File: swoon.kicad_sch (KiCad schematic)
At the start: 93 parts, among them J1 3305-0-15-80-47-27-10-0, J10 3305-0-15-80-47-27-10-0, J11 3305-0-15-80-47-27-10-0, J12 3305-0-15-80-47-27-10-0, J13 3305-0-15-80-47-27-10-0, J14 3305-0-15-80-47-27-10-0, J15 3305-0-15-80-47-27-10-0, J16 3305-0-15-80-47-27-10-0, J17 3305-0-15-80-47-27-10-0, J18 3305-0-15-80-47-27-10-0, J19 3305-0-15-80-47-27-10-0, J2 3305-0-15-80-47-27-10-0, J20 3305-0-15-80-47-27-10-0, J21 3305-0-15-80-47-27-10-0, J22 3305-0-15-80-47-27-10-0, J23 3305-0-15-80-47-27-10-0, J24 3305-0-15-80-47-27-10-0, J25 3305-0-15-80-47-27-10-0, J26 3305-0-15-80-47-27-10-0, J27 3305-0-15-80-47-27-10-0, J28 3305-0-15-80-47-27-10-0, J29 3305-0-15-80-47-27-10-0, J3 3305-0-15-80-47-27-10-0, J30 3305-0-15-80-47-27-10-0, J31 3305-0-15-80-47-27-10-0, J32 3305-0-15-80-47-27-10-0, J33 3305-0-15-80-47-27-10-0, J34 3305-0-15-80-47-27-10-0, J35 3305-0-15-80-47-27-10-0, J36 3305-0-15-80-47-27-10-0, J37 3305-0-15-80-47-27-10-0, J38 3305-0-15-80-47-27-10-0, J39 3305-0-15-80-47-27-10-0, J4 3305-0-15-80-47-27-10-0, J40 3305-0-15-80-47-27-10-0, J41 3305-0-15-80-47-27-10-0, J42 3305-0-15-80-47-27-10-0, J43 3305-0-15-80-47-27-10-0, J44 3305-0-15-80-47-27-10-0, J45 3305-0-15-80-47-27-10-0, J46 3305-0-15-80-47-27-10-0, J47 3305-0-15-80-47-27-10-0, J48 3305-0-15-80-47-27-10-0, J49 3305-0-15-80-47-27-10-0, J5 3305-0-15-80-47-27-10-0, J50 3305-0-15-80-47-27-10-0, J51 3305-0-15-80-47-27-10-0, J52 3305-0-15-80-47-27-10-0, J53 3305-0-15-80-47-27-10-0, J54 3305-0-15-80-47-27-10-0, J55 3305-0-15-80-47-27-10-0, J56 3305-0-15-80-47-27-10-0, J57 3305-0-15-80-47-27-10-0, J58 3305-0-15-80-47-27-10-0, J59 3305-0-15-80-47-27-10-0, J6 3305-0-15-80-47-27-10-0, J60 3305-0-15-80-47-27-10-0, J61 3305-0-15-80-47-27-10-0, J62 3305-0-15-80-47-27-10-0, J63 3305-0-15-80-47-27-10-0, J64 3305-0-15-80-47-27-10-0, J65 3305-0-15-80-47-27-10-0, J66 3305-0-15-80-47-27-10-0, J67 3305-0-15-80-47-27-10-0, J68 3305-0-15-80-47-27-10-0, J69 Conn_01x09_Socket, J7 3305-0-15-80-47-27-10-0, J70 Conn_01x09_Socket, J71 Conn_01x02_Socket, J8 3305-0-15-80-47-27-10-0, J9 3305-0-15-80-47-27-10-0, SW1 SW_Push, SW10 SW_Push, SW11 SW_Push, SW12 SW_Push, SW13 SW_Push, SW14 SW_Push, SW15 SW_Push, SW16 SW_Push, SW17 SW_Push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

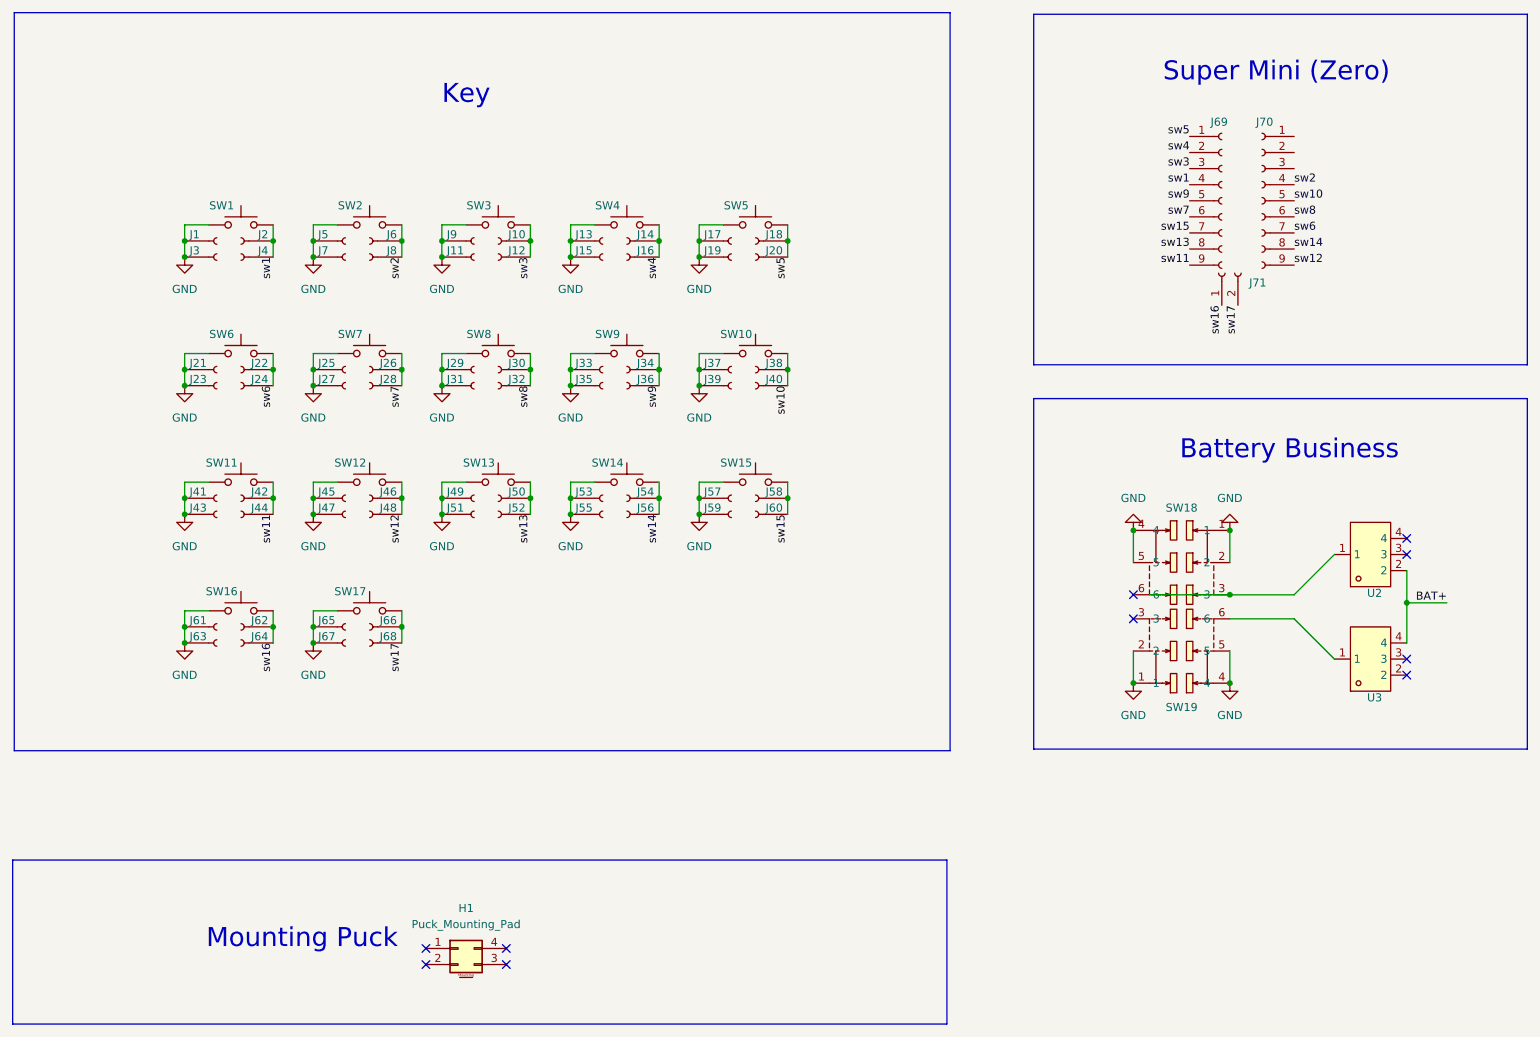
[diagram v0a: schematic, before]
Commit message: Revert "add build123d workflow"
This reverts commit e4690586cedccb0c1d963ceafc7b9e119b231d94.
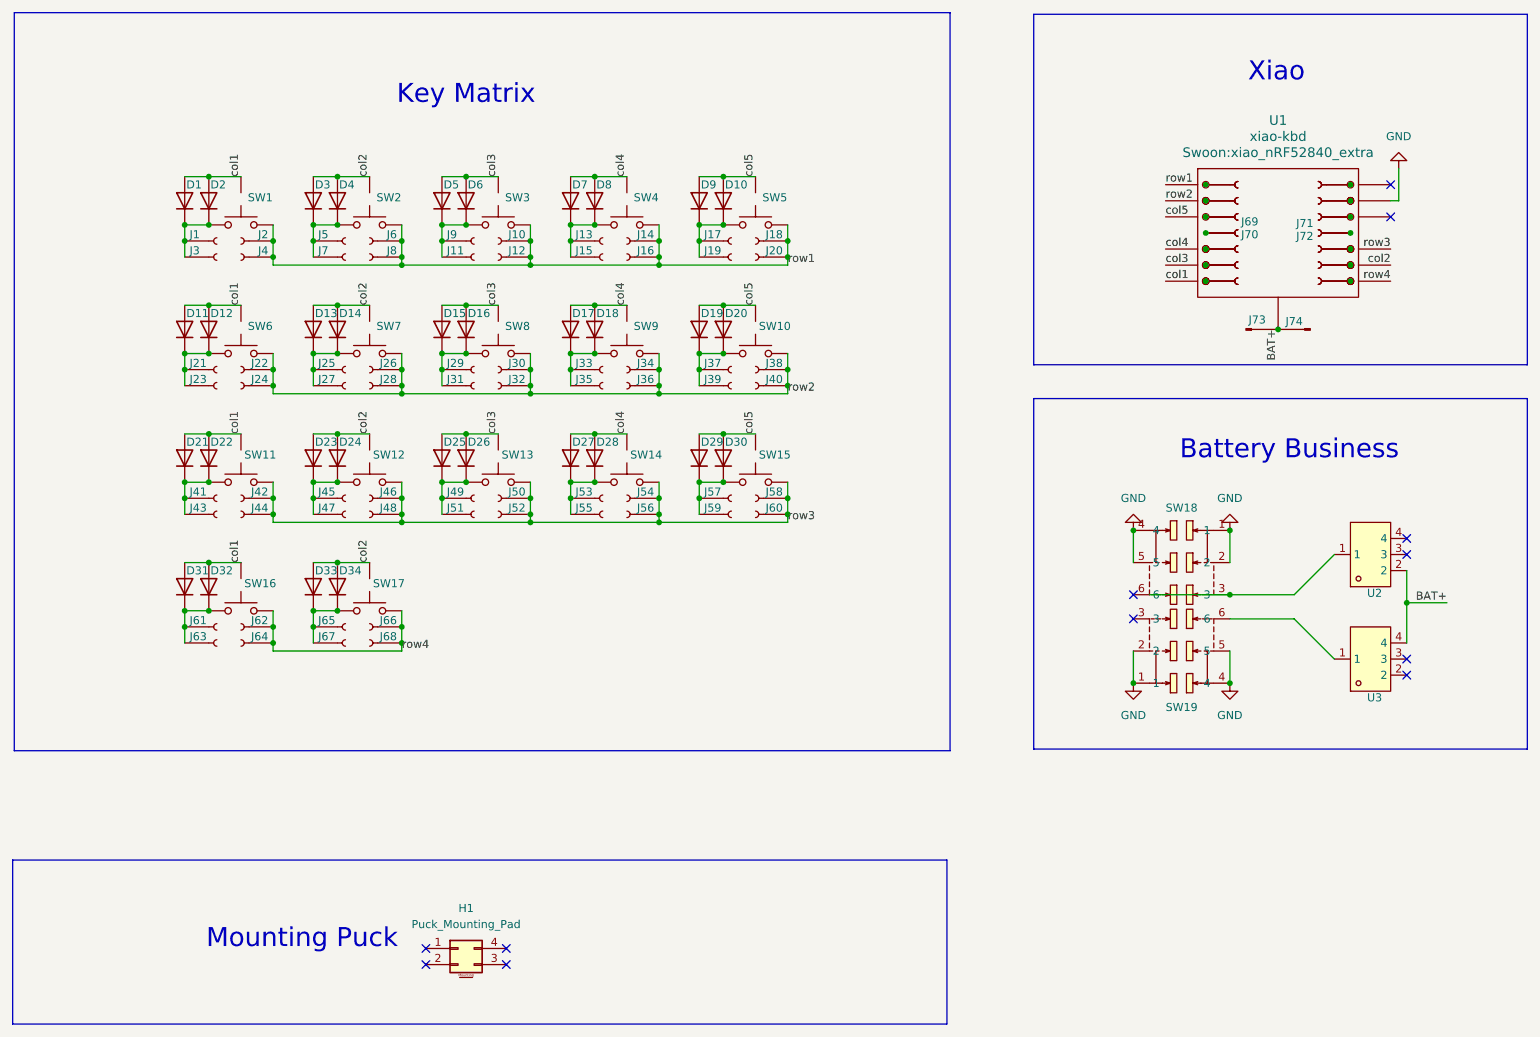
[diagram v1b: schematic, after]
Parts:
- removed J69, J70: Conn_01x09_Socket, Connector_PinHeader_2.54mm:PinHeader_1x09_P2.54mm_Vertical, symbol Connector:Conn_01x09_Socket
- removed J71: Conn_01x02_Socket, Connector_PinHeader_2.54mm:PinHeader_1x02_P2.54mm_Vertical, symbol Connector:Conn_01x02_Socket
- added D1, D10, D11, D12, D13, D14, D15, D16, D17, D18, D19, D2, D20, D21, D22, D23, D24, D25, D26, D27, D28, D29, D3, D30, D31, D32, D33, D34, D4, D5, D6, D7, D8, D9: CD4148WS, Swoon:D_0805_2012Metric, symbol Diode:CD4148W
- added J69, J70, J71, J72: 310-13-107-41-001000, Swoon:MF254V-11-07-0743, symbol Connector:Conn_01x07_Socket
- added J73, J74: Mill Max 0906-2-15-20-75-14-11-0, Swoon:0906-2-15-20-75-14-11-0, symbol Connector:Conn_01x01_Pin
- added TP1, TP10, TP11, TP12, TP13, TP14, TP15, TP16, TP17, TP18, TP19, TP2, TP20, TP3, TP4, TP5, TP6, TP7, TP8, TP9: TestPoint_Small, Swoon:TestPoint_Pad_1.0x1.0mm, symbol Connector:TestPoint_Small
- added U1: xiao-kbd, Swoon:xiao_nRF52840_extra, symbol Swoon:xiao_nRF52840_extra
- SW1, SW10, SW11, SW12, SW13, SW14, SW15, SW16, SW17, SW2, SW3, SW4, SW5, SW6, SW7, SW8, SW9: footprint Swoon:SW_PG1350 -> Swoon:SW_PG1350_vias; symbol Switch:SW_Push -> Swoon:SW_Push; now left out of the parts list
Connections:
- net BAT+: now also J73.1 (Pin_1), J74.1 (Pin_1), U1.15 (BAT+)
- net GND: now also U1.13 (GND); no longer J1.1 (Pin_1), J11.1 (Pin_1), J13.1 (Pin_1), J15.1 (Pin_1), J17.1 (Pin_1), J19.1 (Pin_1), J21.1 (Pin_1), J23.1 (Pin_1), J25.1 (Pin_1), J27.1 (Pin_1), J29.1 (Pin_1), J3.1 (Pin_1), J31.1 (Pin_1), J33.1 (Pin_1), J35.1 (Pin_1), J37.1 (Pin_1), J39.1 (Pin_1), J41.1 (Pin_1), J43.1 (Pin_1), J45.1 (Pin_1), J47.1 (Pin_1), J49.1 (Pin_1), J5.1 (Pin_1), J51.1 (Pin_1), J53.1 (Pin_1), J55.1 (Pin_1), J57.1 (Pin_1), J59.1 (Pin_1), J61.1 (Pin_1), J63.1 (Pin_1), J65.1 (Pin_1), J67.1 (Pin_1), J7.1 (Pin_1), J9.1 (Pin_1), SW1.1, SW10.1, SW11.1, SW12.1, SW13.1, SW14.1, SW15.1, SW16.1, SW17.1, SW2.1, SW3.1, SW4.1, SW5.1, SW6.1, SW7.1, SW8.1, SW9.1
- net sw1 renamed row1
- net row1: now also J10.1 (Pin_1), J12.1 (Pin_1), J14.1 (Pin_1), J16.1 (Pin_1), J18.1 (Pin_1), J20.1 (Pin_1), J6.1 (Pin_1), J8.1 (Pin_1), SW1.1, SW2.1, SW3.1, SW4.1, SW5.1, U1.1 (D0); no longer SW1.2
- net sw10 renamed row2
- net row2: now also J22.1 (Pin_1), J24.1 (Pin_1), J26.1 (Pin_1), J28.1 (Pin_1), J30.1 (Pin_1), J32.1 (Pin_1), J34.1 (Pin_1), J36.1 (Pin_1), SW10.1, SW6.1, SW7.1, SW8.1, SW9.1, U1.2 (D1); no longer SW10.2
- net sw11 renamed row3
- net row3: now also J46.1 (Pin_1), J48.1 (Pin_1), J50.1 (Pin_1), J52.1 (Pin_1), J54.1 (Pin_1), J56.1 (Pin_1), J58.1 (Pin_1), J60.1 (Pin_1), SW11.1, SW12.1, SW13.1, SW14.1, SW15.1, U1.10 (D9); no longer SW11.2
- removed net sw12: J46.1 (Pin_1), J48.1 (Pin_1), SW12.2
- removed net sw13: J50.1 (Pin_1), J52.1 (Pin_1), SW13.2
- removed net sw14: J54.1 (Pin_1), J56.1 (Pin_1), SW14.2
- removed net sw15: J58.1 (Pin_1), J60.1 (Pin_1), SW15.2
- net sw16 renamed row4
- net row4: now also J66.1 (Pin_1), J68.1 (Pin_1), SW16.1, SW17.1, U1.8 (D7); no longer SW16.2
- removed net sw17: J66.1 (Pin_1), J68.1 (Pin_1), SW17.2
- removed net sw2: J6.1 (Pin_1), J8.1 (Pin_1), SW2.2
- removed net sw3: J10.1 (Pin_1), J12.1 (Pin_1), SW3.2
- removed net sw4: J14.1 (Pin_1), J16.1 (Pin_1), SW4.2
- removed net sw5: J18.1 (Pin_1), J20.1 (Pin_1), SW5.2
- removed net sw6: J22.1 (Pin_1), J24.1 (Pin_1), SW6.2
- removed net sw7: J26.1 (Pin_1), J28.1 (Pin_1), SW7.2
- removed net sw8: J30.1 (Pin_1), J32.1 (Pin_1), SW8.2
- removed net sw9: J34.1 (Pin_1), J36.1 (Pin_1), SW9.2
- new net: D31.1 (K), D32.1 (K), J61.1 (Pin_1), J63.1 (Pin_1), SW16.2
- new net: D23.1 (K), D24.1 (K), J45.1 (Pin_1), J47.1 (Pin_1), SW12.2
- new net: J69.1 (Pin_1), J70.1 (Pin_1), TP1.1, U1.16 (hole)
- new net: J69.2 (Pin_2), J70.2 (Pin_2), TP20.1, TP3.1, U1.17 (hole)
- new net: J69.3 (Pin_3), J70.3 (Pin_3), TP5.1, U1.18 (hole)
- new net: J69.4 (Pin_4), J70.4 (Pin_4), U1.19 (hole)
- new net: J69.5 (Pin_5), J70.5 (Pin_5), TP14.1, TP7.1, U1.20 (hole)
- new net: J69.6 (Pin_6), J70.6 (Pin_6), TP16.1, TP9.1, U1.21 (hole)
- new net: J69.7 (Pin_7), J70.7 (Pin_7), TP11.1, TP18.1, U1.22 (hole)
- new net: J71.5 (Pin_5), J72.5 (Pin_5), TP13.1, TP8.1, U1.25 (hole)
- new net: D17.1 (K), D18.1 (K), J33.1 (Pin_1), J35.1 (Pin_1), SW9.2
- new net: D33.1 (K), D34.1 (K), J65.1 (Pin_1), J67.1 (Pin_1), SW17.2
- new net: D19.1 (K), D20.1 (K), J37.1 (Pin_1), J39.1 (Pin_1), SW10.2
- new net: D1.1 (K), D2.1 (K), J1.1 (Pin_1), J3.1 (Pin_1), SW1.2
- new net: D15.1 (K), D16.1 (K), J29.1 (Pin_1), J31.1 (Pin_1), SW8.2
- new net: D29.1 (K), D30.1 (K), J57.1 (Pin_1), J59.1 (Pin_1), SW15.2
- new net: J71.2 (Pin_2), J72.2 (Pin_2), TP19.1, TP4.1, U1.28 (hole)
- new net: D10.1 (K), D9.1 (K), J17.1 (Pin_1), J19.1 (Pin_1), SW5.2
- new net: J71.1 (Pin_1), J72.1 (Pin_1), TP2.1, U1.29 (hole)
- new net: J71.3 (Pin_3), J72.3 (Pin_3), TP6.1, U1.27 (hole)
- new net: J71.4 (Pin_4), J72.4 (Pin_4), U1.26 (hole)
- new net: J71.6 (Pin_6), J72.6 (Pin_6), TP10.1, TP15.1, U1.24 (hole)
- new net: J71.7 (Pin_7), J72.7 (Pin_7), TP12.1, TP17.1, U1.23 (hole)
- new net: D5.1 (K), D6.1 (K), J11.1 (Pin_1), J9.1 (Pin_1), SW3.2
- new net: D27.1 (K), D28.1 (K), J53.1 (Pin_1), J55.1 (Pin_1), SW14.2
- new net: D25.1 (K), D26.1 (K), J49.1 (Pin_1), J51.1 (Pin_1), SW13.2
- new net: D13.1 (K), D14.1 (K), J25.1 (Pin_1), J27.1 (Pin_1), SW7.2
- new net: D3.1 (K), D4.1 (K), J5.1 (Pin_1), J7.1 (Pin_1), SW2.2
- new net: D7.1 (K), D8.1 (K), J13.1 (Pin_1), J15.1 (Pin_1), SW4.2
- new net: D21.1 (K), D22.1 (K), J41.1 (Pin_1), J43.1 (Pin_1), SW11.2
- new net: D11.1 (K), D12.1 (K), J21.1 (Pin_1), J23.1 (Pin_1), SW6.2
- new net col1: D1.2 (A), D11.2 (A), D12.2 (A), D2.2 (A), D21.2 (A), D22.2 (A), D31.2 (A), D32.2 (A), SW1.3, SW11.3, SW16.3, SW6.3, U1.7 (D6)
- new net col2: D13.2 (A), D14.2 (A), D23.2 (A), D24.2 (A), D3.2 (A), D33.2 (A), D34.2 (A), D4.2 (A), SW12.3, SW17.3, SW2.3, SW7.3, U1.9 (D8)
- new net col3: D15.2 (A), D16.2 (A), D25.2 (A), D26.2 (A), D5.2 (A), D6.2 (A), SW13.3, SW3.3, SW8.3, U1.6 (D5)
- new net col4: D17.2 (A), D18.2 (A), D27.2 (A), D28.2 (A), D7.2 (A), D8.2 (A), SW14.3, SW4.3, SW9.3, U1.5 (D4)
- new net col5: D10.2 (A), D19.2 (A), D20.2 (A), D29.2 (A), D30.2 (A), D9.2 (A), SW10.3, SW15.3, SW5.3, U1.3 (D2)
- no-connect marks 10 -> 12
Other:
- note added: "Key Matrix"
- note added: "Xiao"
- note removed: "Key"
- note removed: "Super Mini (Zero)"

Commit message: add build123d workflow
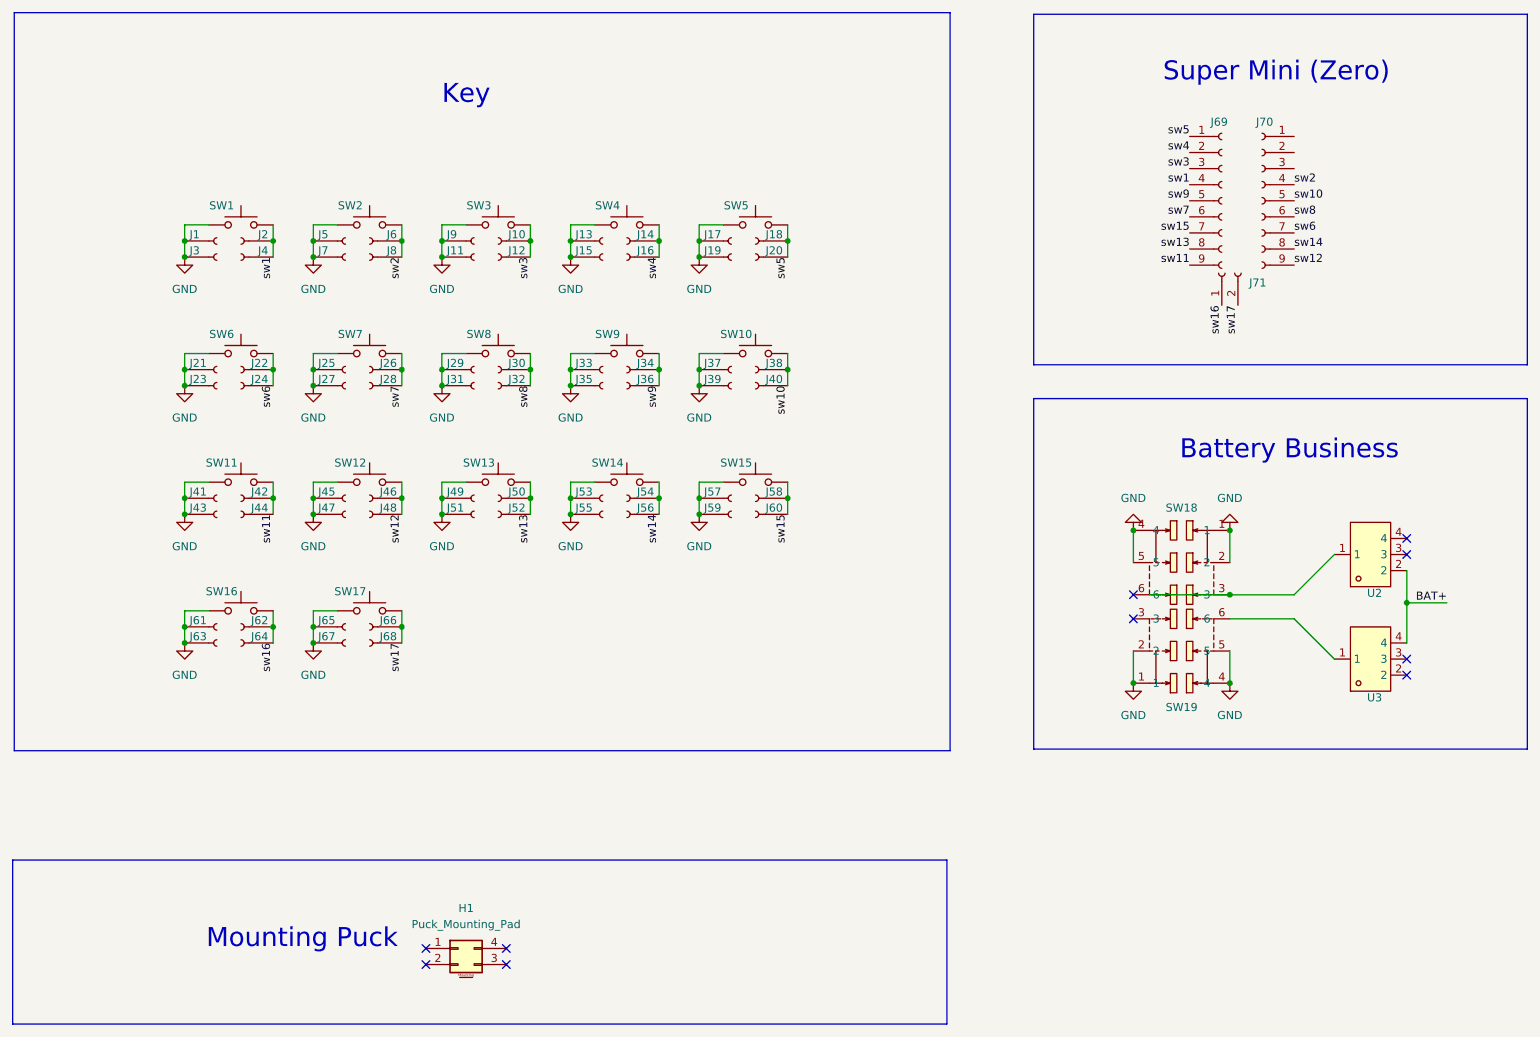
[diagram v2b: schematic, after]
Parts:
- removed D1, D10, D11, D12, D13, D14, D15, D16, D17, D18, D19, D2, D20, D21, D22, D23, D24, D25, D26, D27, D28, D29, D3, D30, D31, D32, D33, D34, D4, D5, D6, D7, D8, D9: CD4148WS, Swoon:D_0805_2012Metric, symbol Diode:CD4148W
- removed J69, J70, J71, J72: 310-13-107-41-001000, Swoon:MF254V-11-07-0743, symbol Connector:Conn_01x07_Socket
- removed J73, J74: Mill Max 0906-2-15-20-75-14-11-0, Swoon:0906-2-15-20-75-14-11-0, symbol Connector:Conn_01x01_Pin
- removed TP1, TP10, TP11, TP12, TP13, TP14, TP15, TP16, TP17, TP18, TP19, TP2, TP20, TP3, TP4, TP5, TP6, TP7, TP8, TP9: TestPoint_Small, Swoon:TestPoint_Pad_1.0x1.0mm, symbol Connector:TestPoint_Small
- removed U1: xiao-kbd, Swoon:xiao_nRF52840_extra, symbol Swoon:xiao_nRF52840_extra
- added J69, J70: Conn_01x09_Socket, Connector_PinHeader_2.54mm:PinHeader_1x09_P2.54mm_Vertical, symbol Connector:Conn_01x09_Socket
- added J71: Conn_01x02_Socket, Connector_PinHeader_2.54mm:PinHeader_1x02_P2.54mm_Vertical, symbol Connector:Conn_01x02_Socket
- SW1, SW10, SW11, SW12, SW13, SW14, SW15, SW16, SW17, SW2, SW3, SW4, SW5, SW6, SW7, SW8, SW9: footprint Swoon:SW_PG1350_vias -> Swoon:SW_PG1350; symbol Swoon:SW_Push -> Switch:SW_Push; now in the parts list
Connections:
- net GND: now also J1.1 (Pin_1), J11.1 (Pin_1), J13.1 (Pin_1), J15.1 (Pin_1), J17.1 (Pin_1), J19.1 (Pin_1), J21.1 (Pin_1), J23.1 (Pin_1), J25.1 (Pin_1), J27.1 (Pin_1), J29.1 (Pin_1), J3.1 (Pin_1), J31.1 (Pin_1), J33.1 (Pin_1), J35.1 (Pin_1), J37.1 (Pin_1), J39.1 (Pin_1), J41.1 (Pin_1), J43.1 (Pin_1), J45.1 (Pin_1), J47.1 (Pin_1), J49.1 (Pin_1), J5.1 (Pin_1), J51.1 (Pin_1), J53.1 (Pin_1), J55.1 (Pin_1), J57.1 (Pin_1), J59.1 (Pin_1), J61.1 (Pin_1), J63.1 (Pin_1), J65.1 (Pin_1), J67.1 (Pin_1), J7.1 (Pin_1), J9.1 (Pin_1), SW1.1, SW10.1, SW11.1, SW12.1, SW13.1, SW14.1, SW15.1, SW16.1, SW17.1, SW2.1, SW3.1, SW4.1, SW5.1, SW6.1, SW7.1, SW8.1, SW9.1
- removed net col1: SW1.3, SW11.3, SW16.3, SW6.3
- removed net col2: SW12.3, SW17.3, SW2.3, SW7.3
- removed net col3: SW13.3, SW3.3, SW8.3
- removed net col4: SW14.3, SW4.3, SW9.3
- removed net col5: SW10.3, SW15.3, SW5.3
- removed net row1: J10.1 (Pin_1), J12.1 (Pin_1), J14.1 (Pin_1), J16.1 (Pin_1), J18.1 (Pin_1), J2.1 (Pin_1), J20.1 (Pin_1), J4.1 (Pin_1), J6.1 (Pin_1), J8.1 (Pin_1), SW1.1, SW2.1, SW3.1, SW4.1, SW5.1
- removed net row2: J22.1 (Pin_1), J24.1 (Pin_1), J26.1 (Pin_1), J28.1 (Pin_1), J30.1 (Pin_1), J32.1 (Pin_1), J34.1 (Pin_1), J36.1 (Pin_1), J38.1 (Pin_1), J40.1 (Pin_1), SW10.1, SW6.1, SW7.1, SW8.1, SW9.1
- removed net row3: J42.1 (Pin_1), J44.1 (Pin_1), J46.1 (Pin_1), J48.1 (Pin_1), J50.1 (Pin_1), J52.1 (Pin_1), J54.1 (Pin_1), J56.1 (Pin_1), J58.1 (Pin_1), J60.1 (Pin_1), SW11.1, SW12.1, SW13.1, SW14.1, SW15.1
- removed net row4: J62.1 (Pin_1), J64.1 (Pin_1), J66.1 (Pin_1), J68.1 (Pin_1), SW16.1, SW17.1
- new net sw1: J2.1 (Pin_1), J4.1 (Pin_1), J69.4 (Pin_4), SW1.2
- new net sw10: J38.1 (Pin_1), J40.1 (Pin_1), J70.5 (Pin_5), SW10.2
- new net sw11: J42.1 (Pin_1), J44.1 (Pin_1), J69.9 (Pin_9), SW11.2
- new net sw12: J46.1 (Pin_1), J48.1 (Pin_1), J70.9 (Pin_9), SW12.2
- new net sw13: J50.1 (Pin_1), J52.1 (Pin_1), J69.8 (Pin_8), SW13.2
- new net sw14: J54.1 (Pin_1), J56.1 (Pin_1), J70.8 (Pin_8), SW14.2
- new net sw15: J58.1 (Pin_1), J60.1 (Pin_1), J69.7 (Pin_7), SW15.2
- new net sw16: J62.1 (Pin_1), J64.1 (Pin_1), J71.1 (Pin_1), SW16.2
- new net sw17: J66.1 (Pin_1), J68.1 (Pin_1), J71.2 (Pin_2), SW17.2
- new net sw2: J6.1 (Pin_1), J70.4 (Pin_4), J8.1 (Pin_1), SW2.2
- new net sw3: J10.1 (Pin_1), J12.1 (Pin_1), J69.3 (Pin_3), SW3.2
- new net sw4: J14.1 (Pin_1), J16.1 (Pin_1), J69.2 (Pin_2), SW4.2
- new net sw5: J18.1 (Pin_1), J20.1 (Pin_1), J69.1 (Pin_1), SW5.2
- new net sw6: J22.1 (Pin_1), J24.1 (Pin_1), J70.7 (Pin_7), SW6.2
- new net sw7: J26.1 (Pin_1), J28.1 (Pin_1), J69.6 (Pin_6), SW7.2
- new net sw8: J30.1 (Pin_1), J32.1 (Pin_1), J70.6 (Pin_6), SW8.2
- new net sw9: J34.1 (Pin_1), J36.1 (Pin_1), J69.5 (Pin_5), SW9.2
- no-connect marks 12 -> 10
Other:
- note added: "Key"
- note added: "Super Mini (Zero)"
- note removed: "Key Matrix"
- note removed: "Xiao"
